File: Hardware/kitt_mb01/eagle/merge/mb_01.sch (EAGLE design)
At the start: 121 parts, among them IC1.01 RT8293A, IC2.00 BQ24266RGET, IC3.01 LSM9DS1, U0.1 SI1922EDH, U6.01 TPS61032RSARPSDO-G16, U7.01 SI1922EDH, U7.2 SI1922EDH, X2.01 S2B-PH-K-S(LF)(SN), X7.02 ARDUINO_UNO, X7.03 CON_HEADER_1X02, X7.05 MOTOR, X7.06 CON_HEADER_1X02, X7.08 CON_HEADER_1X02, X7.09 0R-JUMPA, X7.10 0R-JUMPA, X7.11 CON_HEADER_1X02

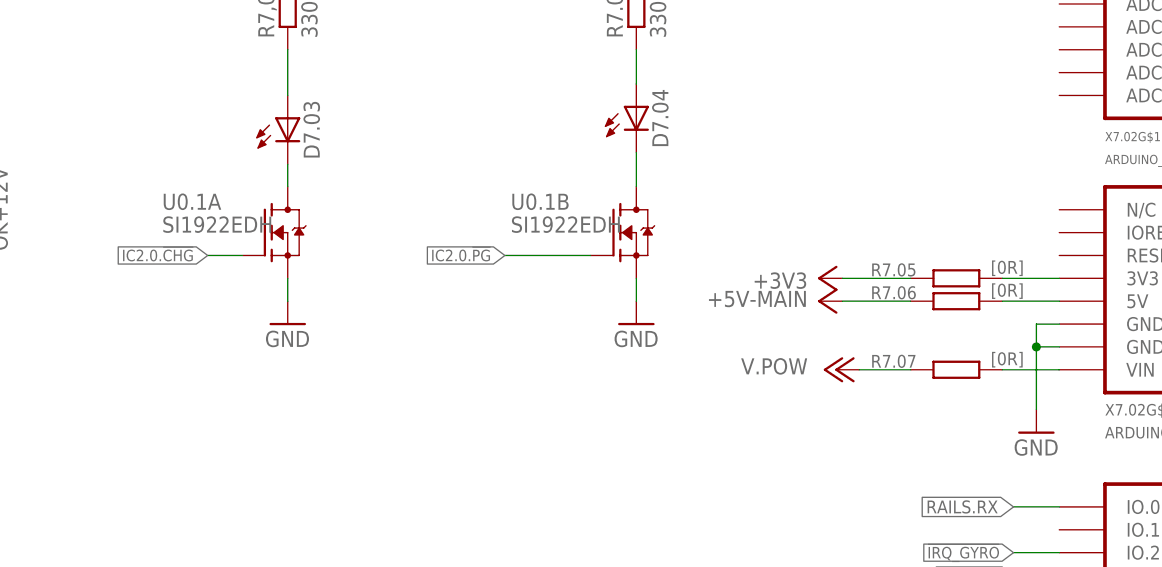
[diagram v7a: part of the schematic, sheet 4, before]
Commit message: updated BOM and board, components have all been selected for this board
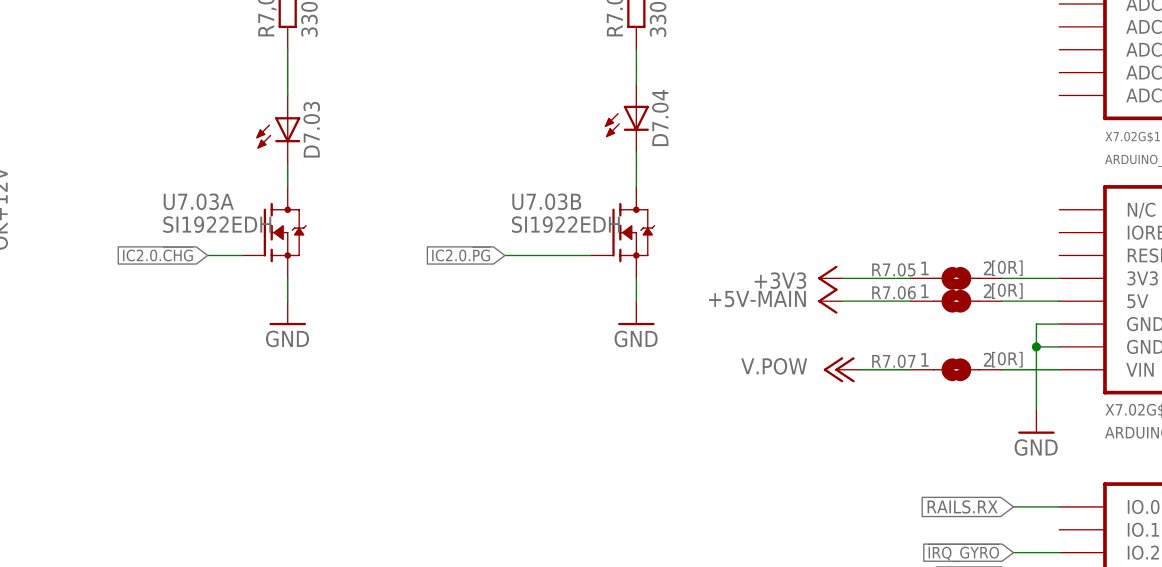
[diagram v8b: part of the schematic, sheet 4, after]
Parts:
- removed L1: (no value), rcl:L-EUL1812
- removed L2.02: BEAD, rcl:L-EUL2012C
- added FB2.01: BEAD, rcl:L-EUL4516C
- C1.04: value XX -> 3.3nF
- C4.03: value (none) -> 4.7uF
- L1.02: value 4.7uH -> 15uH
- R1.02: value XX -> 20kR
- R1.03: value XX -> 62kR
- R1.04: value XX -> 11.8kR
- R7.05, R7.06, R7.07: device rcl:R-EU_R1206 -> jumper:SJ
- renumbered U0.1 to U7.03
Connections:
- net N$16: now also FB2.01.2; no longer L2.02.2
- net N$18: now also FB2.01.1; no longer L2.02.1
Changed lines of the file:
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@@
 <part name="C1.01" library="rcl" deviceset="C-EU" device="C1210K" value="22uF/25V"/>
 <part name="GND3" library="supply1" deviceset="GND" device=""/>
-<part name="L1.02" library="kitt.psvs" deviceset="NRS8030XX" device="" value="4.7uH"/>
+<part name="L1.02" library="kitt.psvs" deviceset="NRS8030XX" device="" value="15uH"/>
 <part name="P+5VMAIN" library="supply1" deviceset="+5V" device="" value="+5V-MAIN"/>
 <part name="FB1.02" library="rcl" deviceset="L-EU" device="L4516C" value="BEAD"/>
@@
 <part name="R1.01" library="rcl" deviceset="R-EU_" device="R0402" value="100kR"/>
 <part name="C1.02" library="rcl" deviceset="C-EU" device="C0402K" value="100nF"/>
-<part name="C1.04" library="rcl" deviceset="C-EU" device="C0402K" value="XX"/>
-<part name="R1.02" library="rcl" deviceset="R-EU_" device="R0402" value="XX"/>
-<part name="R1.03" library="rcl" deviceset="R-EU_" device="R0402" value="XX"/>
-<part name="R1.04" library="rcl" deviceset="R-EU_" device="R0402" value="XX"/>
+<part name="C1.04" library="rcl" deviceset="C-EU" device="C0402K" value="3.3nF"/>
+<part name="R1.02" library="rcl" deviceset="R-EU_" device="R0402" value="20kR"/>
+<part name="R1.03" library="rcl" deviceset="R-EU_" device="R0402" value="62kR"/>
+<part name="R1.04" library="rcl" deviceset="R-EU_" device="R0402" value="11.8kR"/>
 <part name="C1.03" library="rcl" deviceset="C-EU" device="C0402K" value="100nF"/>
 <part name="C1.05" library="rcl" deviceset="C-EU" device="C1206K" value="22uF/6.3V"/>
@@
 <part name="C2.04" library="rcl" deviceset="C-EU" device="C0805" value="33nF/16V"/>
 <part name="GND13" library="supply1" deviceset="GND" device=""/>
-<part name="L2.02" library="rcl" deviceset="L-EU" device="L2012C" value="BEAD"/>
+<part name="FB2.01" library="rcl" deviceset="L-EU" device="L4516C" value="BEAD"/>
 <part name="R2.07" library="rcl" deviceset="R-EU_" device="R0402" value="0R"/>
 <part name="GND14" library="supply1" deviceset="GND" device=""/>
@@
 <part name="C4.01" library="rcl" deviceset="CPOL-EU" device="C/6032-28R" value="47uF/25V"/>
 <part name="C4.02" library="resistor" deviceset="C-EU" device="C0603K" value="100nF/25V"/>
-<part name="C4.03" library="resistor" deviceset="C-EU" device="C0805K"/>
+<part name="C4.03" library="resistor" deviceset="C-EU" device="C0805K" value="4.7uF"/>
 <part name="FB4.01" library="rcl" deviceset="L-EU" device="L4516C" value="BEAD"/>
 <part name="GND21" library="supply1" deviceset="GND" device=""/>
@@
 <part name="R7.11" library="rcl" deviceset="R-EU_" device="R1206" value="SHUNT"/>
 <part name="D7.03" library="led" deviceset="LED" device="CHIPLED_1206"/>
-<part name="U0.1" library="kitt.ic" deviceset="SI1922EDH" device=""/>
+<part name="U7.03" library="kitt.ic" deviceset="SI1922EDH" device=""/>
 <part name="R7,01" library="rcl" deviceset="R-EU_" device="R0603" value="330R"/>
 <part name="R7.01" library="rcl" deviceset="R-EU_" device="R0603" value="330R"/>
@@
 <part name="NTC-" library="wirepad" deviceset="SMD2" device=""/>
 <part name="GND26" library="supply1" deviceset="GND" device=""/>
-<part name="R7.05" library="rcl" deviceset="R-EU_" device="R1206" value="[0R]"/>
-<part name="R7.06" library="rcl" deviceset="R-EU_" device="R1206" value="[0R]"/>
+<part name="R7.05" library="jumper" deviceset="SJ" device="" value="[0R]"/>
+<part name="R7.06" library="jumper" deviceset="SJ" device="" value="[0R]"/>
 <part name="P+5VMAIN2" library="supply1" deviceset="+5V" device="" value="+5V-MAIN"/>
 <part name="+3V6" library="supply1" deviceset="+3V3" device=""/>
-<part name="R7.07" library="rcl" deviceset="R-EU_" device="R1206" value="[0R]"/>
+<part name="R7.07" library="jumper" deviceset="SJ" device="" value="[0R]"/>
 <part name="P+7" library="supply1" deviceset="+12V" device="" value="V.POW"/>
 <part name="X7.08" library="kitt.con" deviceset="CON_HEADER_1X02" device=""/>
@@
 <part name="X7.03" library="kitt.con" deviceset="CON_HEADER_1X02" device=""/>
 <part name="R7.10" library="rcl" deviceset="R-EU_" device="R0603" value="330R"/>
-<part name="L1" library="rcl" deviceset="L-EU" device="L1812"/>
 <part name="L2" library="rcl" deviceset="L-EU" device="L4516C"/>
 </parts>
@@
 </instance>
 <instance part="GND29" gate="1" x="17.78" y="57.15"/>
-<instance part="L1" gate="G$1" x="167.64" y="118.11"/>
 </instances>
 <busses>
@@
 <instance part="C2.04" gate="G$1" x="160.02" y="139.7"/>
 <instance part="GND13" gate="1" x="160.02" y="132.08"/>
-<instance part="L2.02" gate="G$1" x="175.26" y="144.78" rot="MR270"/>
+<instance part="FB2.01" gate="G$1" x="175.26" y="144.78" rot="MR270"/>
 <instance part="R2.07" gate="G$1" x="187.96" y="144.78" rot="MR0"/>
 <instance part="GND14" gate="1" x="132.08" y="99.06" rot="R90"/>
@@
 <wire x1="160.02" y1="144.78" x2="160.02" y2="142.24" width="0.1524" layer="91"/>
 <junction x="149.86" y="144.78"/>
-<pinref part="L2.02" gate="G$1" pin="1"/>
+<pinref part="FB2.01" gate="G$1" pin="1"/>
 <wire x1="170.18" y1="144.78" x2="160.02" y2="144.78" width="0.1524" layer="91"/>
 <junction x="160.02" y="144.78"/>
@@
 <net name="N$16" class="0">
 <segment>
-<pinref part="L2.02" gate="G$1" pin="2"/>
+<pinref part="FB2.01" gate="G$1" pin="2"/>
 <pinref part="R2.07" gate="G$1" pin="2"/>
 <wire x1="180.34" y1="144.78" x2="182.88" y2="144.78" width="0.1524" layer="91"/>
@@
 <instance part="R7.11" gate="G$1" x="35.56" y="149.86"/>
 <instance part="D7.03" gate="G$1" x="130.175" y="144.78"/>
-<instance part="U0.1" gate="A" x="127.635" y="132.08"/>
-<instance part="U0.1" gate="B" x="166.37" y="132.08"/>
+<instance part="U7.03" gate="A" x="127.635" y="132.08"/>
+<instance part="U7.03" gate="B" x="166.37" y="132.08"/>
 <instance part="R7,01" gate="G$1" x="130.175" y="157.48" rot="R90"/>
 <instance part="R7.01" gate="G$1" x="168.91" y="157.48" rot="R90"/>
@@
 <instance part="GND37" gate="1" x="93.345" y="121.285"/>
 <instance part="REF2" gate="G$1" x="209.55" y="26.67"/>
-<instance part="R7.05" gate="G$1" x="204.47" y="127" smashed="yes">
+<instance part="R7.05" gate="1" x="204.47" y="127" smashed="yes">
 <attribute name="NAME" x="194.945" y="127.2286" size="1.4224" layer="95"/>
 <attribute name="VALUE" x="208.28" y="127.508" size="1.4224" layer="96"/>
 </instance>
-<instance part="R7.06" gate="G$1" x="204.47" y="124.46" smashed="yes">
+<instance part="R7.06" gate="1" x="204.47" y="124.46" smashed="yes">
 <attribute name="NAME" x="194.945" y="124.6886" size="1.4224" layer="95"/>
 <attribute name="VALUE" x="208.28" y="124.968" size="1.4224" layer="96"/>
@@
 <attribute name="VALUE" x="187.96" y="127.635" size="1.778" layer="96" rot="R180"/>
 </instance>
-<instance part="R7.07" gate="G$1" x="204.47" y="116.84" smashed="yes">
+<instance part="R7.07" gate="1" x="204.47" y="116.84" smashed="yes">
 <attribute name="NAME" x="194.945" y="117.0686" size="1.4224" layer="95"/>
 <attribute name="VALUE" x="208.28" y="117.348" size="1.4224" layer="96"/>
@@
 </segment>
 <segment>
-<pinref part="U0.1" gate="A" pin="S"/>
+<pinref part="U7.03" gate="A" pin="S"/>
 <pinref part="GND2" gate="1" pin="GND"/>
 <wire x1="130.175" y1="127" x2="130.175" y2="124.46" width="0.1524" layer="91"/>
 </segment>
 <segment>
-<pinref part="U0.1" gate="B" pin="S"/>
+<pinref part="U7.03" gate="B" pin="S"/>
 <pinref part="GND30" gate="1" pin="GND"/>
 <wire x1="168.91" y1="127" x2="168.91" y2="124.46" width="0.1524" layer="91"/>
@@
 </segment>
 <segment>
-<pinref part="R7.06" gate="G$1" pin="1"/>
+<pinref part="R7.06" gate="1" pin="1"/>
 <pinref part="P+5VMAIN2" gate="1" pin="+5V"/>
 <wire x1="191.77" y1="124.46" x2="199.39" y2="124.46" width="0.1524" layer="91"/>
@@
 <segment>
 <pinref part="P+7" gate="1" pin="+12V"/>
-<pinref part="R7.07" gate="G$1" pin="1"/>
+<pinref part="R7.07" gate="1" pin="1"/>
 <wire x1="193.675" y1="116.84" x2="199.39" y2="116.84" width="0.1524" layer="91"/>
 </segment>
@@
 <segment>
 <pinref part="+3V6" gate="G$1" pin="+3V3"/>
-<pinref part="R7.05" gate="G$1" pin="1"/>
+<pinref part="R7.05" gate="1" pin="1"/>
 <wire x1="191.77" y1="127" x2="199.39" y2="127" width="0.1524" layer="91"/>
 </segment>
@@
 <segment>
 <pinref part="D7.03" gate="G$1" pin="C"/>
-<pinref part="U0.1" gate="A" pin="D"/>
+<pinref part="U7.03" gate="A" pin="D"/>
 <wire x1="130.175" y1="139.7" x2="130.175" y2="137.16" width="0.1524" layer="91"/>
 </segment>
@@
 <segment>
 <pinref part="D7.04" gate="G$1" pin="C"/>
-<pinref part="U0.1" gate="B" pin="D"/>
+<pinref part="U7.03" gate="B" pin="D"/>
 <wire x1="168.91" y1="140.97" x2="168.91" y2="137.16" width="0.1524" layer="91"/>
 </segment>
@@
 <segment>
 <label x="121.285" y="129.54" size="1.27" layer="95" rot="R180" xref="yes"/>
-<pinref part="U0.1" gate="A" pin="G"/>
+<pinref part="U7.03" gate="A" pin="G"/>
 <wire x1="121.285" y1="129.54" x2="125.095" y2="129.54" width="0.1524" layer="91"/>
 </segment>
@@
 <wire x1="154.305" y1="129.54" x2="163.83" y2="129.54" width="0.1524" layer="91"/>
 <label x="154.305" y="129.54" size="1.27" layer="95" rot="R180" xref="yes"/>
-<pinref part="U0.1" gate="B" pin="G"/>
+<pinref part="U7.03" gate="B" pin="G"/>
 </segment>
 </net>
@@
 <net name="N$3" class="0">
 <segment>
-<pinref part="R7.05" gate="G$1" pin="2"/>
+<pinref part="R7.05" gate="1" pin="2"/>
 <pinref part="X7.02" gate="G$2" pin="3V3"/>
 <wire x1="209.55" y1="127" x2="215.9" y2="127" width="0.1524" layer="91"/>
@@
 <pinref part="X7.02" gate="G$2" pin="5V"/>
 <wire x1="215.9" y1="124.46" x2="209.55" y2="124.46" width="0.1524" layer="91"/>
-<pinref part="R7.06" gate="G$1" pin="2"/>
+<pinref part="R7.06" gate="1" pin="2"/>
 </segment>
 </net>
 <net name="N$5" class="0">
 <segment>
-<pinref part="R7.07" gate="G$1" pin="2"/>
+<pinref part="R7.07" gate="1" pin="2"/>
 <pinref part="X7.02" gate="G$2" pin="VIN"/>
 <wire x1="209.55" y1="116.84" x2="215.9" y2="116.84" width="0.1524" layer="91"/>
